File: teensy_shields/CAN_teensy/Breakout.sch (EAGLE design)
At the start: 4 parts, among them IC1 SN65HVD230D

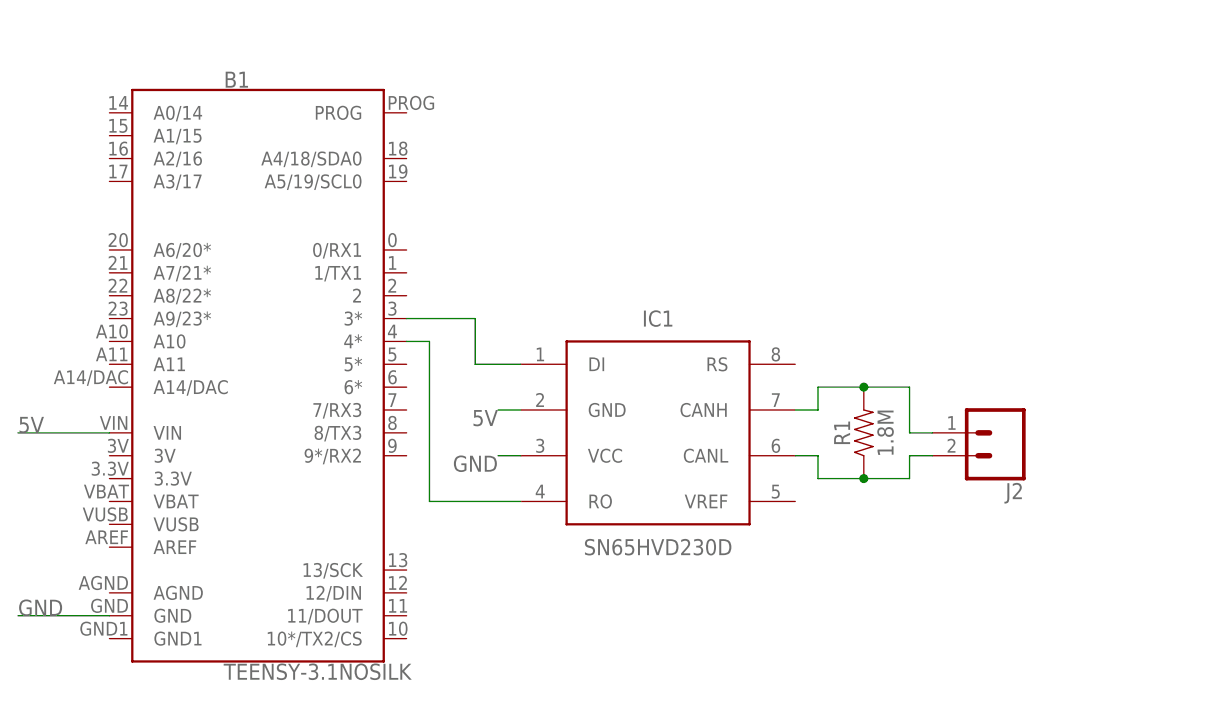
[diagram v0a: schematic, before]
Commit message: updated CAN shield
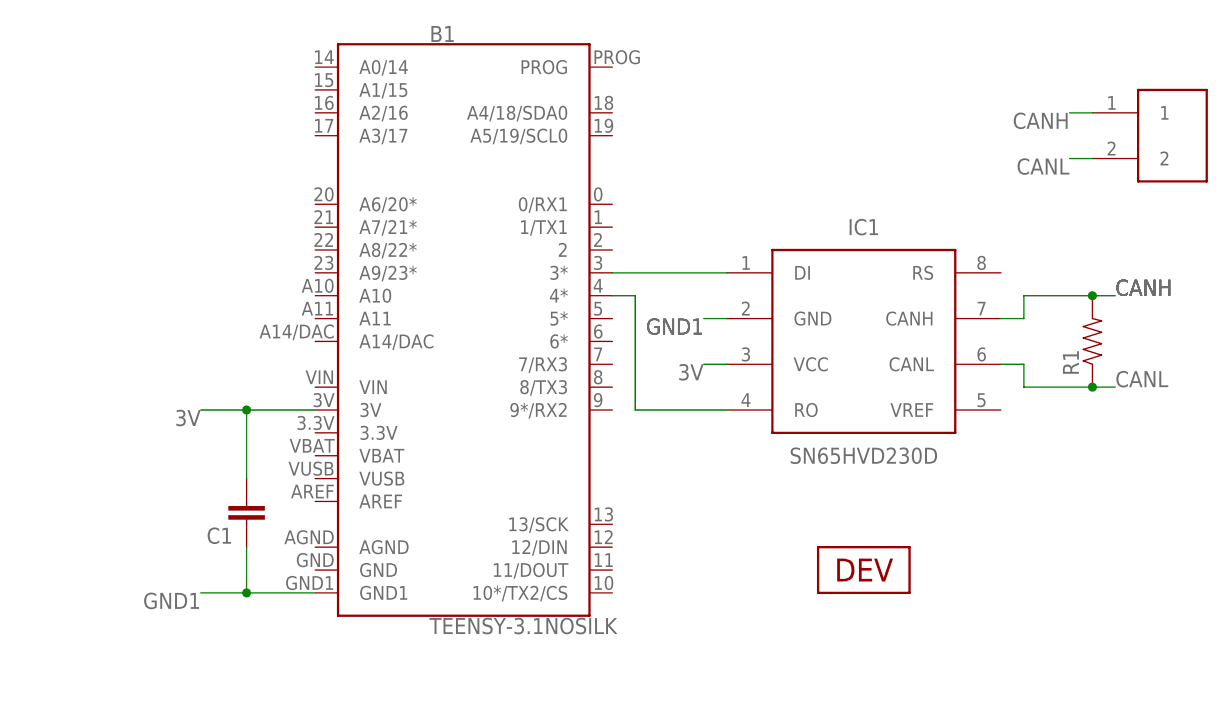
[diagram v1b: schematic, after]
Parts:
- removed J2: (no value), SparkFun-Connectors:CONN_02
- added C1: (no value), SparkFun-Capacitors:CAP0603-CAP
- added U$1: HEADER2, Custom_old:HEADER2
- added U$2: DEV, Custom_old:DEV
- R1: value 1.8M -> (none); device SparkFun-Resistors:1.8MOHM -> SparkFun-Passives:RESISTOR0603-RES
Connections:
- removed net 5V: B1.VIN, IC1.GND
- removed net GND: B1.GND, IC1.VCC
- removed net N$5: IC1.CANL, J2.2, R1.1
- removed net N$6: IC1.CANH, J2.1, R1.2
- new net 3V: B1.3V, C1.2, IC1.VCC
- new net CANH: IC1.CANH, R1.2, U$1.1
- new net CANL: IC1.CANL, R1.1, U$1.2
- new net GND1: B1.GND1, C1.1, IC1.GND
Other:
- moved on the sheet: B1, IC1, R1
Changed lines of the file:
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@@
 </variantdefs>
 <classes>
-<class number="0" name="default" width="0" drill="0">
+<class number="0" name="default" width="0.2032" drill="0">
 </class>
 </classes>
 <parts>
 <part name="IC1" library="Misaka-IC" deviceset="SN65HVD23*D" device="" technology="0"/>
-<part name="J2" library="SparkFun-Connectors" deviceset="CONN_02" device=""/>
 <part name="B1" library="SparkFun-Boards" deviceset="TEENSY-3.1" device="NOSILK"/>
-<part name="R1" library="SparkFun-Resistors" deviceset="1.8MOHM" device="" value="1.8M"/>
+<part name="U$1" library="Custom_old" deviceset="HEADER2" device=""/>
+<part name="R1" library="SparkFun-Passives" deviceset="RESISTOR" device="0603-RES"/>
+<part name="C1" library="SparkFun-Capacitors" deviceset="CAP" device="0603-CAP"/>
+<part name="U$2" library="Custom_old" deviceset="DEV" device=""/>
 </parts>
 <sheets>
@@
 </plain>
 <instances>
-<instance part="IC1" gate="G$1" x="76.2" y="33.02">
-<attribute name="NAME" x="76.2" y="45.72" size="1.778" layer="95" align="center"/>
-<attribute name="VALUE" x="76.2" y="20.32" size="1.778" layer="96" align="center"/>
+<instance part="IC1" gate="G$1" x="99.06" y="43.18">
+<attribute name="NAME" x="99.06" y="55.88" size="1.778" layer="95" align="center"/>
+<attribute name="VALUE" x="99.06" y="30.48" size="1.778" layer="96" align="center"/>
 </instance>
-<instance part="J2" gate="G$1" x="114.3" y="33.02" rot="R180">
-<attribute name="VALUE" x="116.84" y="37.846" size="1.778" layer="96" font="vector" rot="R180"/>
-<attribute name="NAME" x="116.84" y="27.432" size="1.778" layer="95" font="vector" rot="R180"/>
+<instance part="B1" gate="G$1" x="55.88" y="45.72">
+<attribute name="NAME" x="50.8" y="76.454" size="1.778" layer="95" font="vector"/>
+<attribute name="VALUE" x="50.8" y="12.446" size="1.778" layer="96" font="vector" align="top-left"/>
 </instance>
-<instance part="B1" gate="G$1" x="33.02" y="40.64">
-<attribute name="NAME" x="27.94" y="71.374" size="1.778" layer="95" font="vector"/>
-<attribute name="VALUE" x="27.94" y="7.366" size="1.778" layer="96" font="vector" align="top-left"/>
+<instance part="U$1" gate="G$1" x="132.08" y="63.5"/>
+<instance part="R1" gate="G$1" x="124.46" y="43.18" rot="R90">
+<attribute name="NAME" x="122.9614" y="39.37" size="1.778" layer="95" rot="R90"/>
+<attribute name="VALUE" x="127.762" y="39.37" size="1.778" layer="96" rot="R90"/>
 </instance>
-<instance part="R1" gate="G$1" x="99.06" y="33.02" rot="R90">
-<attribute name="NAME" x="97.536" y="33.02" size="1.778" layer="95" font="vector" rot="R90" align="bottom-center"/>
-<attribute name="VALUE" x="100.584" y="33.02" size="1.778" layer="96" font="vector" rot="R90" align="top-center"/>
+<instance part="C1" gate="G$1" x="30.48" y="25.4" rot="R180">
+<attribute name="NAME" x="28.956" y="22.479" size="1.778" layer="95" rot="R180"/>
+<attribute name="VALUE" x="28.956" y="27.559" size="1.778" layer="96" rot="R180"/>
 </instance>
+<instance part="U$2" gate="G$1" x="99.06" y="17.78"/>
 </instances>
 <busses>
 </busses>
 <nets>
-<net name="N$5" class="0">
+<net name="GND1" class="0">
 <segment>
-<pinref part="IC1" gate="G$1" pin="CANL"/>
-<wire x1="91.44" y1="30.48" x2="93.98" y2="30.48" width="0.1524" layer="91"/>
-<wire x1="93.98" y1="30.48" x2="93.98" y2="27.94" width="0.1524" layer="91"/>
-<pinref part="J2" gate="G$1" pin="2"/>
-<wire x1="93.98" y1="27.94" x2="99.06" y2="27.94" width="0.1524" layer="91"/>
-<wire x1="99.06" y1="27.94" x2="104.14" y2="27.94" width="0.1524" layer="91"/>
-<wire x1="104.14" y1="27.94" x2="104.14" y2="30.48" width="0.1524" layer="91"/>
-<wire x1="104.14" y1="30.48" x2="106.68" y2="30.48" width="0.1524" layer="91"/>
-<pinref part="R1" gate="G$1" pin="1"/>
-<junction x="99.06" y="27.94"/>
+<label x="25.4" y="15.24" size="1.778" layer="95" rot="R180"/>
+<pinref part="C1" gate="G$1" pin="1"/>
+<wire x1="30.48" y1="15.24" x2="25.4" y2="15.24" width="0.1524" layer="91"/>
+<wire x1="30.48" y1="15.24" x2="30.48" y2="20.32" width="0.1524" layer="91"/>
+<pinref part="B1" gate="G$1" pin="GND1"/>
+<wire x1="30.48" y1="15.24" x2="38.1" y2="15.24" width="0.1524" layer="91"/>
+<junction x="30.48" y="15.24"/>
+</segment>
+<segment>
+<pinref part="IC1" gate="G$1" pin="GND"/>
+<wire x1="83.82" y1="45.72" x2="81.28" y2="45.72" width="0.1524" layer="91"/>
+<label x="81.28" y="45.72" size="1.778" layer="95" rot="R180"/>
+<label x="81.28" y="45.72" size="1.778" layer="95" rot="R180"/>
 </segment>
 </net>
-<net name="N$6" class="0">
+<net name="N$1" class="0">
 <segment>
-<pinref part="IC1" gate="G$1" pin="CANH"/>
-<wire x1="91.44" y1="35.56" x2="93.98" y2="35.56" width="0.1524" layer="91"/>
-<wire x1="93.98" y1="35.56" x2="93.98" y2="38.1" width="0.1524" layer="91"/>
-<wire x1="93.98" y1="38.1" x2="99.06" y2="38.1" width="0.1524" layer="91"/>
-<wire x1="99.06" y1="38.1" x2="104.14" y2="38.1" width="0.1524" layer="91"/>
-<wire x1="104.14" y1="38.1" x2="104.14" y2="33.02" width="0.1524" layer="91"/>
-<pinref part="J2" gate="G$1" pin="1"/>
-<wire x1="104.14" y1="33.02" x2="106.68" y2="33.02" width="0.1524" layer="91"/>
-<pinref part="R1" gate="G$1" pin="2"/>
-<junction x="99.06" y="38.1"/>
-</segment>
-</net>
-<net name="GND" class="0">
-<segment>
-<pinref part="B1" gate="G$1" pin="GND"/>
-<label x="5.08" y="12.7" size="1.778" layer="95"/>
-<wire x1="15.24" y1="12.7" x2="5.08" y2="12.7" width="0.1524" layer="91"/>
-</segment>
-<segment>
-<pinref part="IC1" gate="G$1" pin="VCC"/>
-<wire x1="60.96" y1="30.48" x2="58.42" y2="30.48" width="0.1524" layer="91"/>
-<label x="58.42" y="30.48" size="1.778" layer="95" rot="R180"/>
+<pinref part="B1" gate="G$1" pin="3*"/>
+<pinref part="IC1" gate="G$1" pin="DI"/>
+<wire x1="71.12" y1="50.8" x2="83.82" y2="50.8" width="0.1524" layer="91"/>
 </segment>
 </net>
 <net name="N$2" class="0">
 <segment>
-<pinref part="B1" gate="G$1" pin="3*"/>
-<wire x1="48.26" y1="45.72" x2="55.88" y2="45.72" width="0.1524" layer="91"/>
-<wire x1="55.88" y1="45.72" x2="55.88" y2="40.64" width="0.1524" layer="91"/>
-<pinref part="IC1" gate="G$1" pin="DI"/>
-<wire x1="55.88" y1="40.64" x2="60.96" y2="40.64" width="0.1524" layer="91"/>
+<pinref part="B1" gate="G$1" pin="4*"/>
+<wire x1="71.12" y1="48.26" x2="73.66" y2="48.26" width="0.1524" layer="91"/>
+<wire x1="73.66" y1="48.26" x2="73.66" y2="35.56" width="0.1524" layer="91"/>
+<pinref part="IC1" gate="G$1" pin="RO"/>
+<wire x1="73.66" y1="35.56" x2="83.82" y2="35.56" width="0.1524" layer="91"/>
 </segment>
 </net>
-<net name="N$3" class="0">
+<net name="CANH" class="0">
 <segment>
-<pinref part="B1" gate="G$1" pin="4*"/>
-<wire x1="48.26" y1="43.18" x2="50.8" y2="43.18" width="0.1524" layer="91"/>
-<wire x1="50.8" y1="43.18" x2="50.8" y2="25.4" width="0.1524" layer="91"/>
-<pinref part="IC1" gate="G$1" pin="RO"/>
-<wire x1="50.8" y1="25.4" x2="60.96" y2="25.4" width="0.1524" layer="91"/>
+<pinref part="IC1" gate="G$1" pin="CANH"/>
+<wire x1="114.3" y1="45.72" x2="116.84" y2="45.72" width="0.1524" layer="91"/>
+<wire x1="116.84" y1="45.72" x2="116.84" y2="48.26" width="0.1524" layer="91"/>
+<pinref part="R1" gate="G$1" pin="2"/>
+<wire x1="116.84" y1="48.26" x2="124.46" y2="48.26" width="0.1524" layer="91"/>
+<wire x1="124.46" y1="48.26" x2="127" y2="48.26" width="0.1524" layer="91"/>
+<junction x="124.46" y="48.26"/>
+<label x="127" y="48.26" size="1.778" layer="95"/>
+<label x="127" y="48.26" size="1.778" layer="95"/>
+<label x="127" y="48.26" size="1.778" layer="95"/>
+</segment>
+<segment>
+<pinref part="U$1" gate="G$1" pin="1"/>
+<wire x1="124.46" y1="68.58" x2="121.92" y2="68.58" width="0.1524" layer="91"/>
+<label x="121.92" y="68.58" size="1.778" layer="95" rot="R180"/>
 </segment>
 </net>
-<net name="5V" class="0">
+<net name="CANL" class="0">
 <segment>
-<pinref part="B1" gate="G$1" pin="VIN"/>
-<label x="5.08" y="33.02" size="1.778" layer="95"/>
-<wire x1="15.24" y1="33.02" x2="5.08" y2="33.02" width="0.1524" layer="91"/>
+<pinref part="IC1" gate="G$1" pin="CANL"/>
+<wire x1="114.3" y1="40.64" x2="116.84" y2="40.64" width="0.1524" layer="91"/>
+<wire x1="116.84" y1="40.64" x2="116.84" y2="38.1" width="0.1524" layer="91"/>
+<pinref part="R1" gate="G$1" pin="1"/>
+<wire x1="116.84" y1="38.1" x2="124.46" y2="38.1" width="0.1524" layer="91"/>
+<wire x1="124.46" y1="38.1" x2="127" y2="38.1" width="0.1524" layer="91"/>
+<junction x="124.46" y="38.1"/>
+<label x="127" y="38.1" size="1.778" layer="95"/>
 </segment>
 <segment>
-<pinref part="IC1" gate="G$1" pin="GND"/>
-<wire x1="60.96" y1="35.56" x2="58.42" y2="35.56" width="0.1524" layer="91"/>
-<label x="58.42" y="35.56" size="1.778" layer="95" rot="R180"/>
+<pinref part="U$1" gate="G$1" pin="2"/>
+<wire x1="124.46" y1="63.5" x2="121.92" y2="63.5" width="0.1524" layer="91"/>
+<label x="121.92" y="63.5" size="1.778" layer="95" rot="R180"/>
 </segment>
 </net>
+<net name="3V" class="0">
+<segment>
+<pinref part="IC1" gate="G$1" pin="VCC"/>
+<wire x1="83.82" y1="40.64" x2="81.28" y2="40.64" width="0.1524" layer="91"/>
+<label x="81.28" y="40.64" size="1.778" layer="95" rot="R180"/>
+</segment>
+<segment>
+<label x="25.4" y="35.56" size="1.778" layer="95" rot="R180"/>
+<pinref part="C1" gate="G$1" pin="2"/>
+<wire x1="30.48" y1="35.56" x2="25.4" y2="35.56" width="0.1524" layer="91"/>
+<wire x1="30.48" y1="27.94" x2="30.48" y2="35.56" width="0.1524" layer="91"/>
+<pinref part="B1" gate="G$1" pin="3V"/>
+<wire x1="30.48" y1="35.56" x2="38.1" y2="35.56" width="0.1524" layer="91"/>
+<junction x="30.48" y="35.56"/>
+</segment>
+</net>

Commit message: cleanup
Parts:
- R1: value (none) -> 120
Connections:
- removed net GND1: B1.GND1, C1.1, IC1.GND
- new net EN_CAN: B1.2, IC1.RS
- new net GND: B1.AGND, B1.GND, B1.GND1, C1.1, IC1.GND
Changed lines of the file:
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@@
 <?xml version="1.0" encoding="utf-8"?>
 <!DOCTYPE eagle SYSTEM "eagle.dtd">
-<eagle version="9.2.0">
+<eagle version="9.1.1">
 <drawing>
 <settings>
@@
 <part name="B1" library="SparkFun-Boards" deviceset="TEENSY-3.1" device="NOSILK"/>
 <part name="U$1" library="Custom_old" deviceset="HEADER2" device=""/>
-<part name="R1" library="SparkFun-Passives" deviceset="RESISTOR" device="0603-RES"/>
+<part name="R1" library="SparkFun-Passives" deviceset="RESISTOR" device="0603-RES" value="120"/>
 <part name="C1" library="SparkFun-Capacitors" deviceset="CAP" device="0603-CAP"/>
 <part name="U$2" library="Custom_old" deviceset="DEV" device=""/>
@@
 </busses>
 <nets>
-<net name="GND1" class="0">
-<segment>
-<label x="25.4" y="15.24" size="1.778" layer="95" rot="R180"/>
-<pinref part="C1" gate="G$1" pin="1"/>
-<wire x1="30.48" y1="15.24" x2="25.4" y2="15.24" width="0.1524" layer="91"/>
-<wire x1="30.48" y1="15.24" x2="30.48" y2="20.32" width="0.1524" layer="91"/>
-<pinref part="B1" gate="G$1" pin="GND1"/>
-<wire x1="30.48" y1="15.24" x2="38.1" y2="15.24" width="0.1524" layer="91"/>
-<junction x="30.48" y="15.24"/>
-</segment>
-<segment>
-<pinref part="IC1" gate="G$1" pin="GND"/>
-<wire x1="83.82" y1="45.72" x2="81.28" y2="45.72" width="0.1524" layer="91"/>
-<label x="81.28" y="45.72" size="1.778" layer="95" rot="R180"/>
-<label x="81.28" y="45.72" size="1.778" layer="95" rot="R180"/>
-</segment>
-</net>
 <net name="N$1" class="0">
 <segment>
@@
 </segment>
 </net>
+<net name="EN_CAN" class="0">
+<segment>
+<pinref part="IC1" gate="G$1" pin="RS"/>
+<wire x1="114.3" y1="50.8" x2="124.46" y2="50.8" width="0.1524" layer="91"/>
+<label x="116.84" y="50.8" size="1.778" layer="95"/>
+</segment>
+<segment>
+<pinref part="B1" gate="G$1" pin="2"/>
+<wire x1="71.12" y1="53.34" x2="73.66" y2="53.34" width="0.1524" layer="91"/>
+<label x="73.66" y="53.34" size="1.27" layer="95" xref="yes"/>
+</segment>
+</net>
+<net name="GND" class="0">
+<segment>
+<label x="25.4" y="15.24" size="1.778" layer="95" rot="R180"/>
+<pinref part="C1" gate="G$1" pin="1"/>
+<wire x1="30.48" y1="15.24" x2="25.4" y2="15.24" width="0.1524" layer="91"/>
+<wire x1="30.48" y1="15.24" x2="30.48" y2="20.32" width="0.1524" layer="91"/>
+<pinref part="B1" gate="G$1" pin="GND1"/>
+<wire x1="30.48" y1="15.24" x2="38.1" y2="15.24" width="0.1524" layer="91"/>
+<junction x="30.48" y="15.24"/>
+<pinref part="B1" gate="G$1" pin="GND"/>
+<wire x1="38.1" y1="17.78" x2="38.1" y2="15.24" width="0.1524" layer="91"/>
+<junction x="38.1" y="15.24"/>
+<pinref part="B1" gate="G$1" pin="AGND"/>
+<wire x1="38.1" y1="17.78" x2="38.1" y2="20.32" width="0.1524" layer="91"/>
+<junction x="38.1" y="17.78"/>
+</segment>
+<segment>
+<pinref part="IC1" gate="G$1" pin="GND"/>
+<wire x1="83.82" y1="45.72" x2="81.28" y2="45.72" width="0.1524" layer="91"/>
+<label x="81.28" y="45.72" size="1.778" layer="95" rot="R180"/>
+<label x="81.28" y="45.72" size="1.778" layer="95" rot="R180"/>
+</segment>
+</net>
